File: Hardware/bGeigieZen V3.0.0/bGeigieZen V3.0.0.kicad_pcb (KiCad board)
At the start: 2 copper layers, 129.4 x 64.6 mm, 29 parts, among them J1 M5 2x15 pin, J10 QI GND, J11 QI charger Plus, J2 Geiger, J3 GPS, J4 Geiger 2, J5 Extra support header, J6 Grove, J7 Grove, J8 QI charger ground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

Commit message: Updated and newly routed  V3.0.0 board
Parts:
- G back: renamed from G***
- G front: renamed from G***
- moved C1 6.37 mm to (198.0, 78.2)
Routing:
- net 3.3V: track 0.00 -> 137.6 mm
- net /GIO2 on Core and GIO32 on Core-2: track 0.00 -> 108.1 mm
- net /BAT: track 0.00 -> 94.6 mm
- net /Reset: track 0.00 -> 83.8 mm, vias 0 -> 2
- net /SCL: track 0.00 -> 71.7 mm, vias 0 -> 1
- net /VBATT: track 0.00 -> 65.4 mm
- net Net-(BT1--): track 0.00 -> 64.4 mm, vias 0 -> 1
- net /SDA: track 0.00 -> 60.1 mm, vias 0 -> 1
- net /TX2: track 0.00 -> 42.1 mm, vias 0 -> 1
- net /RX2: track 0.00 -> 41.0 mm, vias 0 -> 1
- net Net-(J9-Pin_1): track 0.00 -> 2.54 mm
- net GND: vias 0 -> 2

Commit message: Updated V3.0.0 board
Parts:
- removed sea of pads 1: PinHeader_2x13_P2.54mm_Vertical, bGeigieZen:PinHeader_2x13_P2.54mm_Vertical
- removed sea of pads 2: PinHeader_2x13_P2.54mm_Vertical, bGeigieZen:PinHeader_2x13_P2.54mm_Vertical
- added 1850 LABEL: LOGO, bGeigieRaku_M5_1015:18650 map, B.Cu at (178.0, 117.1)
- J11: footprint Connector_PinHeader_2.54mm:PinHeader_1x02_P2.54mm_Vertical -> bGeigieZen:PinHeader_1x02_P2.54mm_Vertical_4056
- moved J11 2.29 mm to (182.7, 105.1), turned to 180 degrees
- turned J8 to 0 degrees
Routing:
- net /SCL: track 71.7 -> 83.5 mm
- net /Reset: track 83.8 -> 87.7 mm
- net Net-(BT1--): track 64.4 -> 61.3 mm, vias 1 -> 0
- net 3.3V: track 137.6 -> 140.5 mm, vias 0 -> 1
- net /SDA: track 60.1 -> 61.6 mm, vias 1 -> 2
- net /GIO2 on Core and GIO32 on Core-2: track 108.1 -> 109.1 mm

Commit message: Cleaned out V3.0.0 board..
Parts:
- removed C1: 47uF, bGeigieZen:C025-024X044
- removed H1, H10, H2, H3, H5, H7, H8, H9: MountingHole_Pad, MountingHole:MountingHole_3.2mm_M3
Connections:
- J1 pad 5: /Reset -> unconnected-(J1-Pin_5-Pad5)
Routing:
- net /Reset: track 87.7 -> 0.00 mm, vias 2 -> 0
- net /SCL: track 83.5 -> 67.2 mm, vias 1 -> 0
- net /SDA: track 61.6 -> 51.6 mm
- net 3.3V: track 140.5 -> 136.8 mm
- net /GIO2 on Core and GIO32 on Core-2: track 109.1 -> 111.8 mm, vias 0 -> 2
- net Net-(BT1--): track 61.3 -> 59.6 mm
- net GND: track 0.00 -> 1.26 mm, vias 2 -> 1
- net /VBATT: track 65.7 -> 66.3 mm
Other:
- board text removed: "+"
- board text removed: "-"

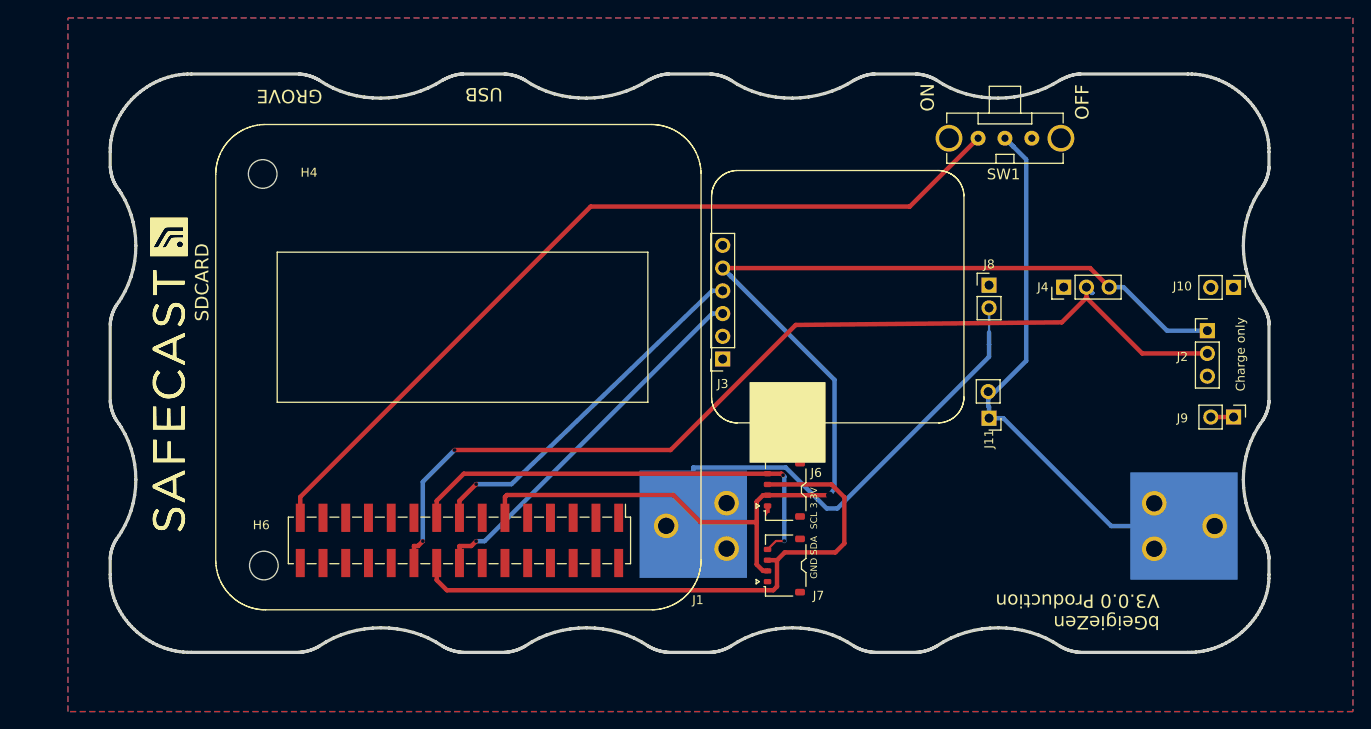
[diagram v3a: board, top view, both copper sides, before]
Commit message: Added SDCard files
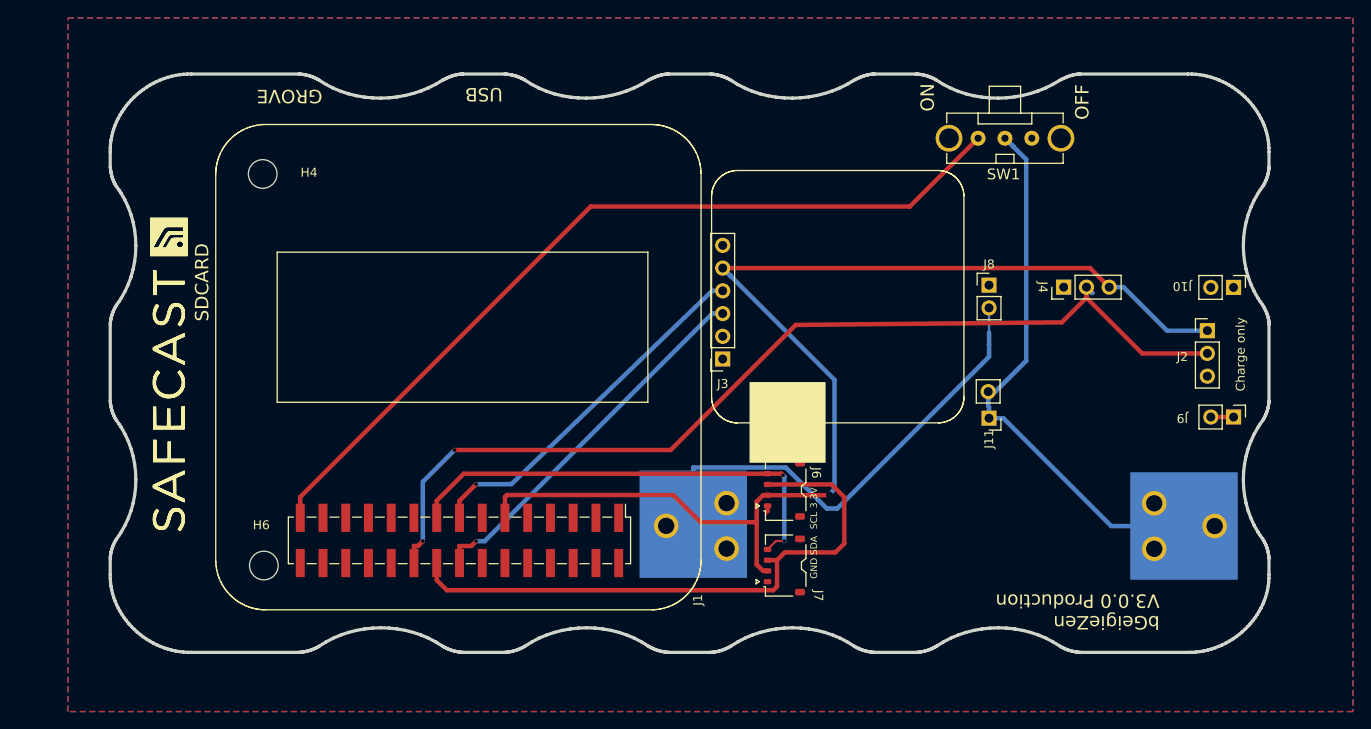
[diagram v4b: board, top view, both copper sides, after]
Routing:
- net Net-(BT1--): track 59.6 -> 58.9 mm
